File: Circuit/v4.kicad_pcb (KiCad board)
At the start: 2 copper layers, 30 x 50 mm, 52 parts, among them J2 AVR-ISP-6, Q1 AO3400A, U1 EL3H7(B)(TA)-G

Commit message: Update thermistor to NCP15WB473F03RC
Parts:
- D1: value AZ432ANTR-E1 -> TL432G-A-AE3-R
- R19: value NCP18WB473J03RB -> NTC THERMISTOR 47KOHMS 4050K; footprint Resistors_SMD:R_0603 -> Resistors_SMD:R_0402
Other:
- board text added: "JLCJLCJLCJLC"
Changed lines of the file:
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@@
   (general
     (thickness 1.6)
-    (drawings 27)
-    (tracks 367)
+    (drawings 30)
+    (tracks 369)
     (zones 0)
     (modules 52)
@@
     (34 B.Paste user)
     (35 F.Paste user)
-    (36 B.SilkS user)
+    (36 B.SilkS user hide)
     (37 F.SilkS user)
     (38 B.Mask user hide)
-    (39 F.Mask user)
+    (39 F.Mask user hide)
     (40 Dwgs.User user)
     (41 Cmts.User user)
@@
     (add_net "Net-(R7-Pad2)")
   )
+  (module Resistors_SMD:R_0402 (layer F.Cu)
+    (at 114.0176 82.5876 90)
+    (descr "Resistor SMD 0402, reflow soldering, Vishay (see dcrcw.pdf)")
+    (tags "resistor 0402")
+    (attr smd)
+    (fp_text reference R19 (at 0 -1.35 90) (layer F.SilkS)
+      (effects (font (size 1 1) (thickness 0.15)))
+    )
+    (fp_text value "NTC THERMISTOR 47KOHMS 4050K" (at 0 1.45 90) (layer F.Fab)
+      (effects (font (size 1 1) (thickness 0.15)))
+    )
+    (fp_text user %R (at 0 -1.35 90) (layer F.Fab)
+      (effects (font (size 1 1) (thickness 0.15)))
+    )
+    (fp_line (start -0.5 0.25) (end -0.5 -0.25) (layer F.Fab) (width 0.1))
+    (fp_line (start 0.5 0.25) (end -0.5 0.25) (layer F.Fab) (width 0.1))
+    (fp_line (start 0.5 -0.25) (end 0.5 0.25) (layer F.Fab) (width 0.1))
+    (fp_line (start -0.5 -0.25) (end 0.5 -0.25) (layer F.Fab) (width 0.1))
+    (fp_line (start 0.25 -0.53) (end -0.25 -0.53) (layer F.SilkS) (width 0.12))
+    (fp_line (start -0.25 0.53) (end 0.25 0.53) (layer F.SilkS) (width 0.12))
+    (fp_line (start -0.8 -0.45) (end 0.8 -0.45) (layer F.CrtYd) (width 0.05))
+    (fp_line (start -0.8 -0.45) (end -0.8 0.45) (layer F.CrtYd) (width 0.05))
+    (fp_line (start 0.8 0.45) (end 0.8 -0.45) (layer F.CrtYd) (width 0.05))
+    (fp_line (start 0.8 0.45) (end -0.8 0.45) (layer F.CrtYd) (width 0.05))
+    (pad 1 smd rect (at -0.45 0 90) (size 0.4 0.6) (layers F.Cu F.Paste F.Mask)
+      (net 15 2_VOLT))
+    (pad 2 smd rect (at 0.45 0 90) (size 0.4 0.6) (layers F.Cu F.Paste F.Mask)
+      (net 27 "Net-(ATTINY841-Pad9)"))
+    (model ${KISYS3DMOD}/Resistors_SMD.3dshapes/R_0402.wrl
+      (at (xyz 0 0 0))
+      (scale (xyz 1 1 1))
+      (rotate (xyz 0 0 0))
+    )
+  )
   (module TO_SOT_Packages_SMD:SOT-23 (layer F.Cu)
     (at 124.7176 58.7876 90)
@@
       (effects (font (size 1 1) (thickness 0.15)))
     )
-    (fp_text value AZ432ANTR-E1 (at 0 2.5 90) (layer F.Fab)
+    (fp_text value TL432G-A-AE3-R (at 0 2.5 90) (layer F.Fab)
       (effects (font (size 1 1) (thickness 0.15)))
     )
@@
     (pad 2 smd rect (at 0.75 0) (size 0.5 0.9) (layers F.Cu F.Paste F.Mask)
       (net 1 GND))
-    (model ${KISYS3DMOD}/Resistors_SMD.3dshapes/R_0603.wrl
-      (at (xyz 0 0 0))
-      (scale (xyz 1 1 1))
-      (rotate (xyz 0 0 0))
-    )
-  )
-  (module Resistors_SMD:R_0603 (layer F.Cu)
-    (at 114.0176 82.5876 90)
-    (descr "Resistor SMD 0603, reflow soldering, Vishay (see dcrcw.pdf)")
-    (tags "resistor 0603")
-    (attr smd)
-    (fp_text reference R19 (at 2.233333 0.05 270) (layer F.SilkS)
-      (effects (font (size 0.7 0.7) (thickness 0.1)))
-    )
-    (fp_text value NCP18WB473J03RB (at 0 1.5 90) (layer F.Fab)
-      (effects (font (size 0.7 0.7) (thickness 0.1)))
-    )
-    (fp_text user %R (at 0 0 90) (layer F.Fab)
-      (effects (font (size 0.7 0.7) (thickness 0.1)))
-    )
-    (fp_line (start -0.8 0.4) (end -0.8 -0.4) (layer F.Fab) (width 0.1))
-    (fp_line (start 0.8 0.4) (end -0.8 0.4) (layer F.Fab) (width 0.1))
-    (fp_line (start 0.8 -0.4) (end 0.8 0.4) (layer F.Fab) (width 0.1))
-    (fp_line (start -0.8 -0.4) (end 0.8 -0.4) (layer F.Fab) (width 0.1))
-    (fp_line (start 0.5 0.68) (end -0.5 0.68) (layer F.SilkS) (width 0.12))
-    (fp_line (start -0.5 -0.68) (end 0.5 -0.68) (layer F.SilkS) (width 0.12))
-    (fp_line (start -1.25 -0.7) (end 1.25 -0.7) (layer F.CrtYd) (width 0.05))
-    (fp_line (start -1.25 -0.7) (end -1.25 0.7) (layer F.CrtYd) (width 0.05))
-    (fp_line (start 1.25 0.7) (end 1.25 -0.7) (layer F.CrtYd) (width 0.05))
-    (fp_line (start 1.25 0.7) (end -1.25 0.7) (layer F.CrtYd) (width 0.05))
-    (pad 1 smd rect (at -0.75 0 90) (size 0.5 0.9) (layers F.Cu F.Paste F.Mask)
-      (net 15 2_VOLT))
-    (pad 2 smd rect (at 0.75 0 90) (size 0.5 0.9) (layers F.Cu F.Paste F.Mask)
-      (net 27 "Net-(ATTINY841-Pad9)"))
     (model ${KISYS3DMOD}/Resistors_SMD.3dshapes/R_0603.wrl
       (at (xyz 0 0 0))
@@
     )
   )
+  (gr_text JLCJLCJLCJLC (at 102.9176 60.2376 90) (layer F.SilkS)
+    (effects (font (size 0.7 0.7) (thickness 0.17)))
+  )
+  (gr_text 1 (at 105.1676 71.4876) (layer F.SilkS)
+    (effects (font (size 1 1) (thickness 0.2)))
+  )
+  (gr_text 1 (at 123.9176 61.2376) (layer F.SilkS)
+    (effects (font (size 1 1) (thickness 0.2)))
+  )
   (gr_text + (at 123.5176 88.9876) (layer F.SilkS)
     (effects (font (size 1.5 1.5) (thickness 0.3)))
@@
   (gr_line (start 131.9176 49.4876) (end 131.9176 96.4876) (layer Edge.Cuts) (width 0.15))
   (gr_line (start 103.4176 47.9876) (end 130.4176 47.9876) (layer Edge.Cuts) (width 0.15))
-  (gr_text 1 (at 115.9176 57.7876) (layer F.SilkS)
-    (effects (font (size 1.2 1.2) (thickness 0.2)))
+  (gr_text 1 (at 112.4176 57.4876) (layer F.SilkS)
+    (effects (font (size 1 1) (thickness 0.2)))
   )
   (gr_text TX (at 122.3176 49.1876) (layer B.SilkS)
@@
   (segment (start 119.442894 66.962306) (end 118.408132 66.962306) (width 0.3) (layer B.Cu) (net 15))
   (via (at 114.0176 83.8876) (size 0.8) (drill 0.4) (layers F.Cu B.Cu) (net 15))
-  (segment (start 114.0176 83.3376) (end 114.0176 83.8876) (width 0.3) (layer F.Cu) (net 15))
   (segment (start 115.9176 78.6876) (end 115.9176 74.137738) (width 0.3) (layer B.Cu) (net 15))
   (segment (start 112.8176 81.7876) (end 115.9176 78.6876) (width 0.3) (layer B.Cu) (net 15))
@@
   (segment (start 114.0176 83.8876) (end 112.8176 82.6876) (width 0.3) (layer B.Cu) (net 15))
   (segment (start 112.8176 82.6876) (end 112.8176 81.7876) (width 0.3) (layer B.Cu) (net 15))
+  (segment (start 114.0176 83.0376) (end 114.0176 83.8876) (width 0.3) (layer F.Cu) (net 15))
   (via (at 124.5176 69.7876) (size 0.8) (drill 0.4) (layers F.Cu B.Cu) (net 16))
   (segment (start 126.8176 69.6576) (end 124.6476 69.6576) (width 0.3) (layer F.Cu) (net 16) (status 10))
@@
   (segment (start 112.617599 87.087601) (end 115.1176 84.5876) (width 0.3) (layer B.Cu) (net 27))
   (segment (start 112.617599 91.377599) (end 112.617599 87.087601) (width 0.3) (layer B.Cu) (net 27))
+  (segment (start 114.017596 82.137596) (end 114.0176 82.1376) (width 0.3) (layer F.Cu) (net 27))
+  (segment (start 114.017596 81.837596) (end 114.017596 82.137596) (width 0.3) (layer F.Cu) (net 27))
   (segment (start 118.7676 86.6876) (end 120.3676 86.6876) (width 1) (layer F.Cu) (net 28) (status 30))
   (segment (start 118.7676 84.0376) (end 120.3676 84.0376) (width 1) (layer F.Cu) (net 29) (status 30))

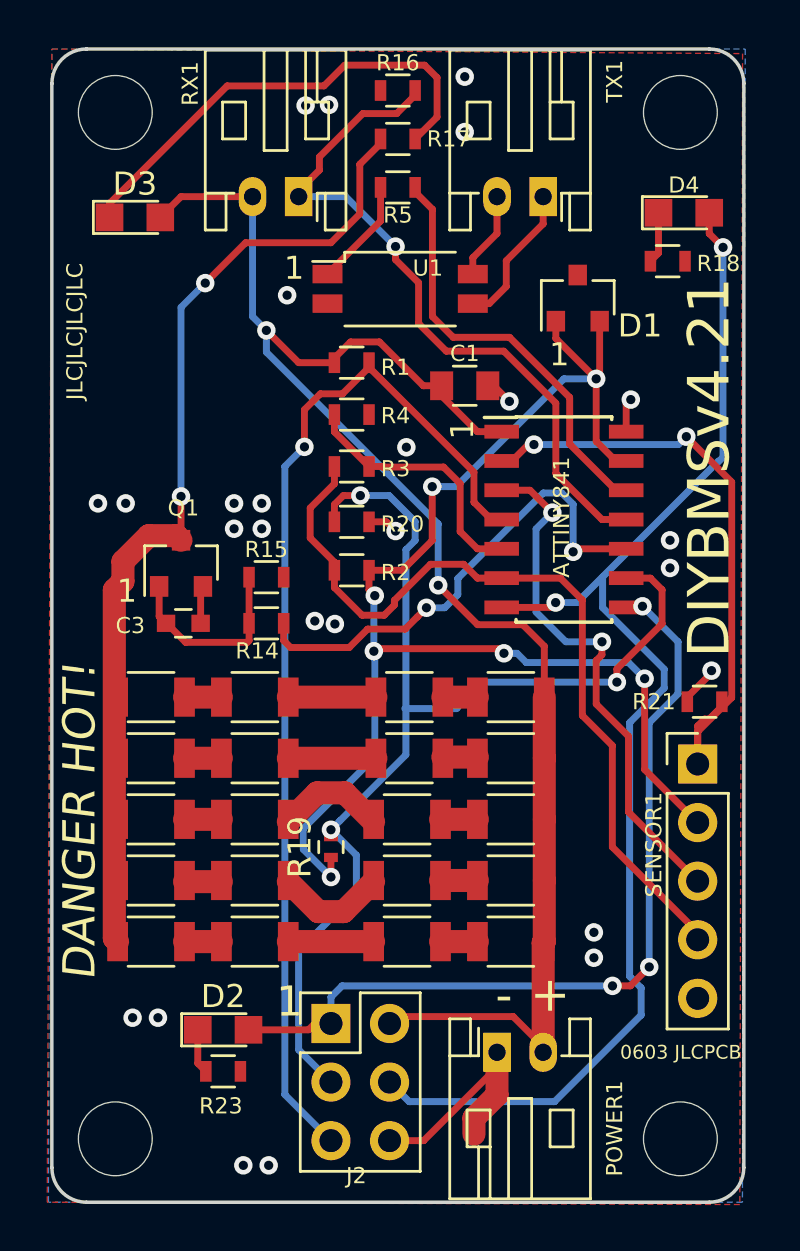
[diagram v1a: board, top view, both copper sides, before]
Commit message: Added JLCPCB assembly mounting holes
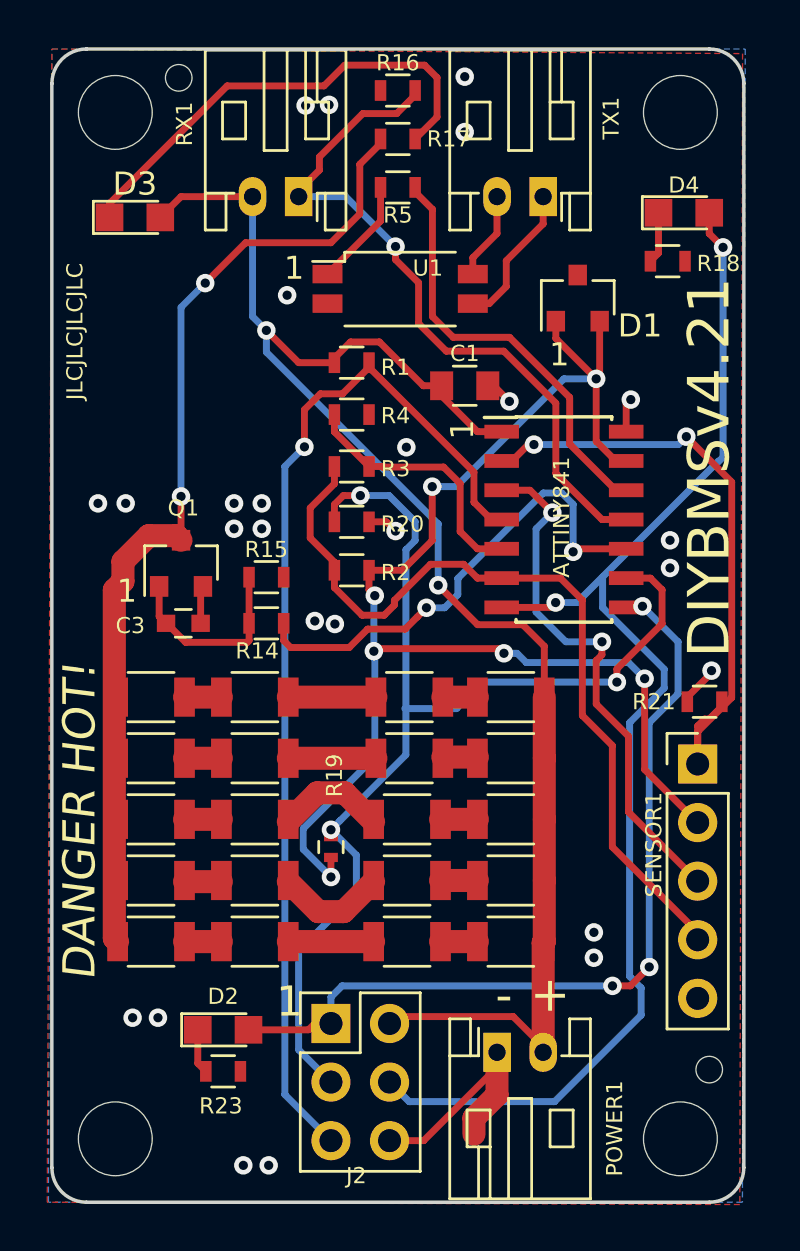
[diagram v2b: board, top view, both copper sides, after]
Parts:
- added REF**: JLCAssemblyHole_1_152mm, Mounting_Holes:MountingHole_2.5mm, F.Cu at (107.4, 49.2)
- added REF**: JLCAssemblyHole_1_152mm, Mounting_Holes:MountingHole_2.5mm, F.Cu at (130.4, 92.2)
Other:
- board text removed: "0603 JLCPCB"
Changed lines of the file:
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@@
   (general
     (thickness 1.6)
-    (drawings 30)
+    (drawings 29)
     (tracks 369)
     (zones 0)
-    (modules 52)
+    (modules 54)
     (nets 38)
   )
   (page A4)
   (layers
-    (0 F.Cu signal)
-    (31 B.Cu signal)
+    (0 F.Cu signal hide)
+    (31 B.Cu signal hide)
     (32 B.Adhes user)
     (33 F.Adhes user hide)
@@
     (add_net "Net-(R7-Pad2)")
   )
+  (module Mounting_Holes:MountingHole_2.5mm (layer F.Cu)
+    (at 107.4176 49.2376)
+    (descr "Mounting Hole 2.5mm, no annular")
+    (tags "mounting hole 2.5mm no annular")
+    (attr virtual)
+    (fp_text reference REF** (at 0 -3.5) (layer F.SilkS) hide
+      (effects (font (size 1 1) (thickness 0.15)))
+    )
+    (fp_text value JLCAssemblyHole_1_152mm (at 0 3.5) (layer F.Fab)
+      (effects (font (size 1 1) (thickness 0.15)))
+    )
+    (fp_circle (center 0 0) (end 1.16 0) (layer F.CrtYd) (width 0.05))
+    (fp_circle (center 0 0) (end 1.16 0) (layer Cmts.User) (width 0.15))
+    (fp_text user %R (at 0.3 1.9) (layer F.Fab)
+      (effects (font (size 1 1) (thickness 0.15)))
+    )
+    (pad "" np_thru_hole circle (at 0 0) (size 1.152 1.152) (drill 1.152) (layers *.Cu *.Mask))
+  )
+  (module Mounting_Holes:MountingHole_2.5mm locked (layer F.Cu)
+    (at 130.4176 92.2376)
+    (descr "Mounting Hole 2.5mm, no annular")
+    (tags "mounting hole 2.5mm no annular")
+    (attr virtual)
+    (fp_text reference REF** (at 7.5 0.5) (layer F.SilkS) hide
+      (effects (font (size 1 1) (thickness 0.15)))
+    )
+    (fp_text value JLCAssemblyHole_1_152mm (at 0 3.5) (layer F.Fab)
+      (effects (font (size 1 1) (thickness 0.15)))
+    )
+    (fp_text user %R (at 0.3 1.9) (layer F.Fab)
+      (effects (font (size 1 1) (thickness 0.15)))
+    )
+    (fp_circle (center 0 0) (end 1.16 0) (layer Cmts.User) (width 0.15))
+    (fp_circle (center 0 0) (end 1.16 0) (layer F.CrtYd) (width 0.05))
+    (pad "" np_thru_hole circle (at 0 0) (size 1.152 1.152) (drill 1.152) (layers *.Cu *.Mask))
+  )
   (module Resistors_SMD:R_0402 (layer F.Cu)
     (at 114.0176 82.5876 90)
@@
     (tags "resistor 0402")
     (attr smd)
-    (fp_text reference R19 (at 0 -1.35 90) (layer F.SilkS)
-      (effects (font (size 1 1) (thickness 0.15)))
+    (fp_text reference R19 (at 3.1 0.15 90) (layer F.SilkS)
+      (effects (font (size 0.7 0.7) (thickness 0.15)))
     )
     (fp_text value "NTC THERMISTOR 47KOHMS 4050K" (at 0 1.45 90) (layer F.Fab)
@@
     (attr smd)
     (fp_text reference D2 (at 0 -1.45) (layer F.SilkS)
-      (effects (font (size 1 1) (thickness 0.15)))
+      (effects (font (size 0.7 0.7) (thickness 0.1)))
     )
     (fp_text value Blue (at 0 1.55) (layer F.Fab)
@@
     (descr "JST PH series connector, S2B-PH-K, side entry type, through hole, Datasheet: http://www.jst-mfg.com/product/pdf/eng/ePH.pdf")
     (tags "connector jst ph")
-    (fp_text reference TX1 (at -3.1 5 270) (layer F.SilkS)
+    (fp_text reference TX1 (at -2.95 3.4 270) (layer F.SilkS)
       (effects (font (size 0.7 0.7) (thickness 0.1)))
     )
@@
     (tags "mounting hole 3.2mm no annular m3")
     (attr virtual)
-    (fp_text reference REF** (at -10.3848 -2.9492) (layer F.SilkS) hide
+    (fp_text reference REF** (at -5.5 0) (layer F.SilkS) hide
       (effects (font (size 0.7 0.7) (thickness 0.1)))
     )
@@
     (descr "JST PH series connector, S2B-PH-K, side entry type, through hole, Datasheet: http://www.jst-mfg.com/product/pdf/eng/ePH.pdf")
     (tags "connector jst ph")
-    (fp_text reference RX1 (at 4.7 4.9 270) (layer F.SilkS)
+    (fp_text reference RX1 (at 4.95 3.15 270) (layer F.SilkS)
       (effects (font (size 0.7 0.7) (thickness 0.1)))
     )
@@
     (effects (font (size 1.5 1.5) (thickness 0.3)))
   )
-  (gr_text "0603 JLCPCB" (at 131.8176 91.4876) (layer F.SilkS)
-    (effects (font (size 0.6 0.6) (thickness 0.1)) (justify right))
-  )
   (gr_arc (start 130.4176 96.4876) (end 130.4176 97.9876) (angle -90) (layer Edge.Cuts) (width 0.15))
